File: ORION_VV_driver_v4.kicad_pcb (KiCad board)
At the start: 4 copper layers, 52.4 x 123.1 mm, 146 parts, among them J11 Conn_01x02, J12 Conn_01x05, J13 Conn_01x05, J15 Conn_01x02, J2 Conn_01x04, J3 Conn_01x04, J4 Conn_01x06, J5 Conn_01x07, J6 Conn_01x07, Q1 IRF8721PBF-1, Q10 IRF8721PBF-1, Q11 IRF8721PBF-1, Q12 IRF8721PBF-1, Q2 IRF8721PBF-1, Q3 IRF8721PBF-1, Q4 IRF8721PBF-1, Q5 IRF8721PBF-1, Q6 IRF8721PBF-1, Q7 IRF8721PBF-1, Q8 IRF8721PBF-1, Q9 IRF8721PBF-1, SW1 SW_Push, SW2 SW_Push, SW3 SW_Push, SW4 SW_Push, SW5 SW_Push, U1 BD9G101G, U2 L78L33_SOT89, U3 MAX3051, U5 INA199, U6 INA199, Y1 Resonator

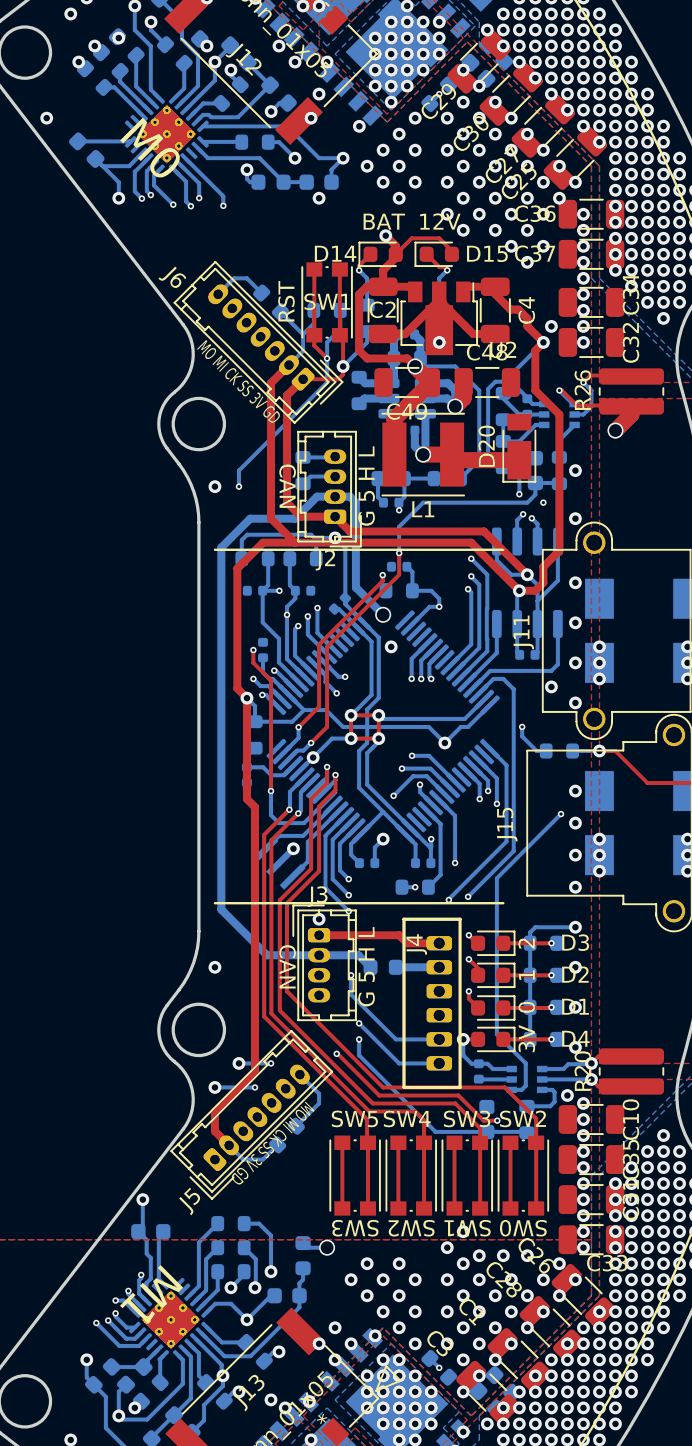
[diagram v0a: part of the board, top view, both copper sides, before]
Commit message: 配線とシルクの改善
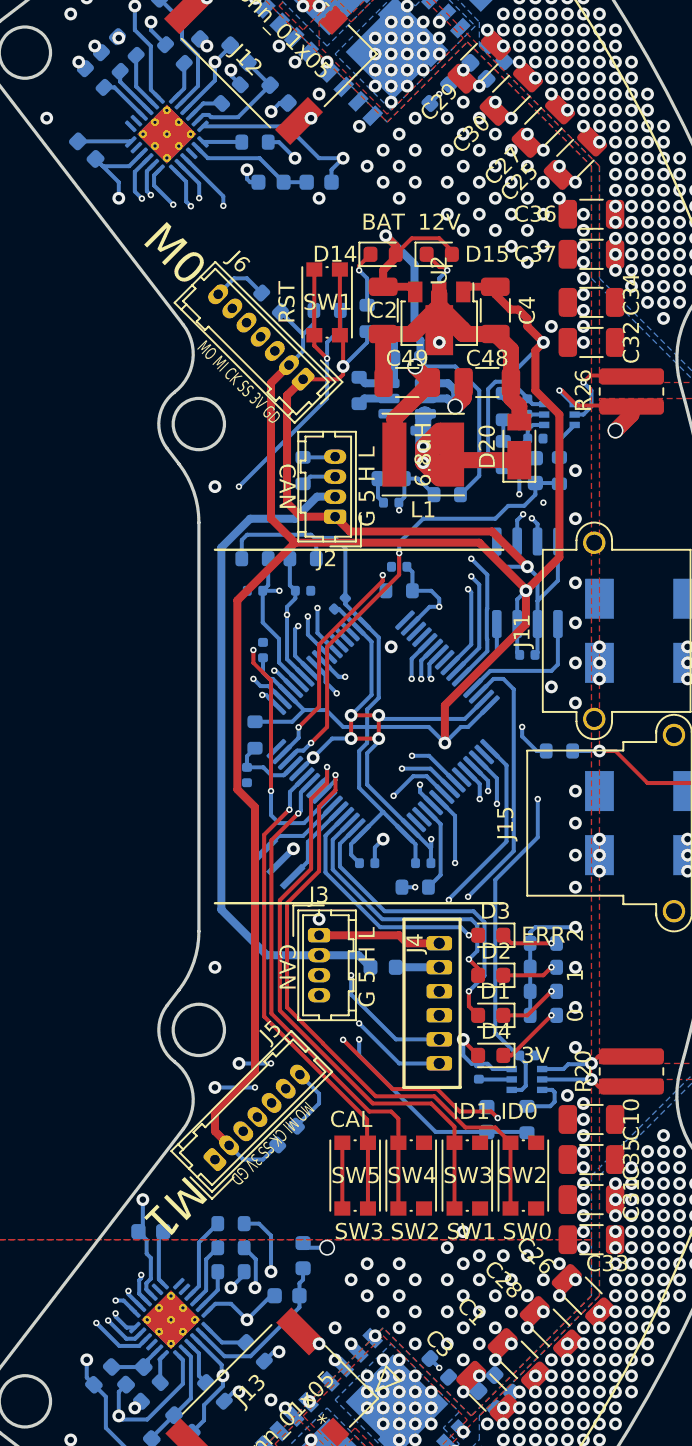
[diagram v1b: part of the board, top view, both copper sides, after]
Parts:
- added C53: 0.1u, Capacitor_SMD:C_0402_1005Metric, B.Cu at (121.0, 82.0)
- added C54: 0.1u, Capacitor_SMD:C_0402_1005Metric, B.Cu at (120.5, 120.5)
- moved R4 1.50 mm to (121.5, 118.0)
- moved D4 1.00 mm to (118.2, 120.5)
- moved R1 1.00 mm to (121.5, 116.5)
- moved R34 1.00 mm to (115.5, 85.5)
- moved D3 0.50 mm to (118.2, 113.0)
- moved R2 0.50 mm to (121.5, 115.0)
- moved D1 0.46 mm to (118.2, 118.0)
- turned SW2 to -90 degrees
- turned SW3 to -90 degrees
- turned SW4 to -90 degrees
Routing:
- net +5V: track 51.0 -> 41.8 mm, vias 1 -> 0
- net +3V3: track 206.0 -> 214.7 mm, vias 6 -> 4
- net GND: track 153.7 -> 159.4 mm
- net +BATT: track 48.4 -> 44.6 mm
- net Net-(C46-Pad1): track 10.5 -> 13.8 mm, vias 1 -> 2
- net /SW0: track 40.7 -> 38.9 mm
- net /SW2: track 33.2 -> 31.7 mm
- net /SW1: track 38.6 -> 37.0 mm
- net Net-(D4-Pad1): track 3.33 -> 4.36 mm
- net /LED_2: track 15.9 -> 15.1 mm, vias 2 -> 1
- net +9V: track 198.0 -> 197.2 mm
- net /TEMP_FET_1: track 67.1 -> 66.5 mm
- net Net-(D1-Pad1): track 3.34 -> 3.95 mm
- net /M0_CS: track 29.3 -> 28.7 mm
- net /LED_1: track 17.8 -> 17.4 mm, vias 2 -> 1
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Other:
- board text added: "6.8uH"
- board text added: "CAL"
- board text added: "ERR"
- board text added: "ID0"
- board text added: "ID1"

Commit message: 微調整
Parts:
- added J1: Conn_01x01, TestPoint:TestPoint_Pad_D1.0mm, F.Cu at (104.5, 69.5)
- added J10: Conn_01x01, TestPoint:TestPoint_Pad_D1.0mm, F.Cu at (103.0, 130.5)
- added J14: Conn_01x01, TestPoint:TestPoint_Pad_D1.0mm, F.Cu at (105.0, 130.5)
- added J7: Conn_01x01, TestPoint:TestPoint_Pad_D1.0mm, F.Cu at (102.5, 69.5)
- added J8: Conn_01x01, TestPoint:TestPoint_Pad_D1.0mm, F.Cu at (100.5, 69.5)
- added J9: Conn_01x01, TestPoint:TestPoint_Pad_D1.0mm, F.Cu at (101.0, 130.5)
- moved C14 2.06 mm to (118.5, 79.5)
- moved R9 2.06 mm to (118.5, 82.0)
- moved R8 1.12 mm to (118.5, 84.0), turned to 0 degrees
- moved C23 0.97 mm to (117.0, 124.5)
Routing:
- net /M1_WL: track 49.4 -> 60.2 mm
- net /M1_VL: track 51.0 -> 61.6 mm
- net /M1_UL: track 53.3 -> 63.2 mm
- net /M0_UL: track 43.6 -> 50.6 mm
- net /M0_VL: track 42.2 -> 48.9 mm
- net /M0_WL: track 41.7 -> 46.8 mm
- net GND: track 159.4 -> 160.6 mm
- net +9V: track 197.2 -> 196.4 mm
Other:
- board text added: "9V"
- board text added: "B"
- board text added: "G"
- board text added: "R"
- board text added: "UL VL WL"
- board text added: "W"
- board text removed: "12V"

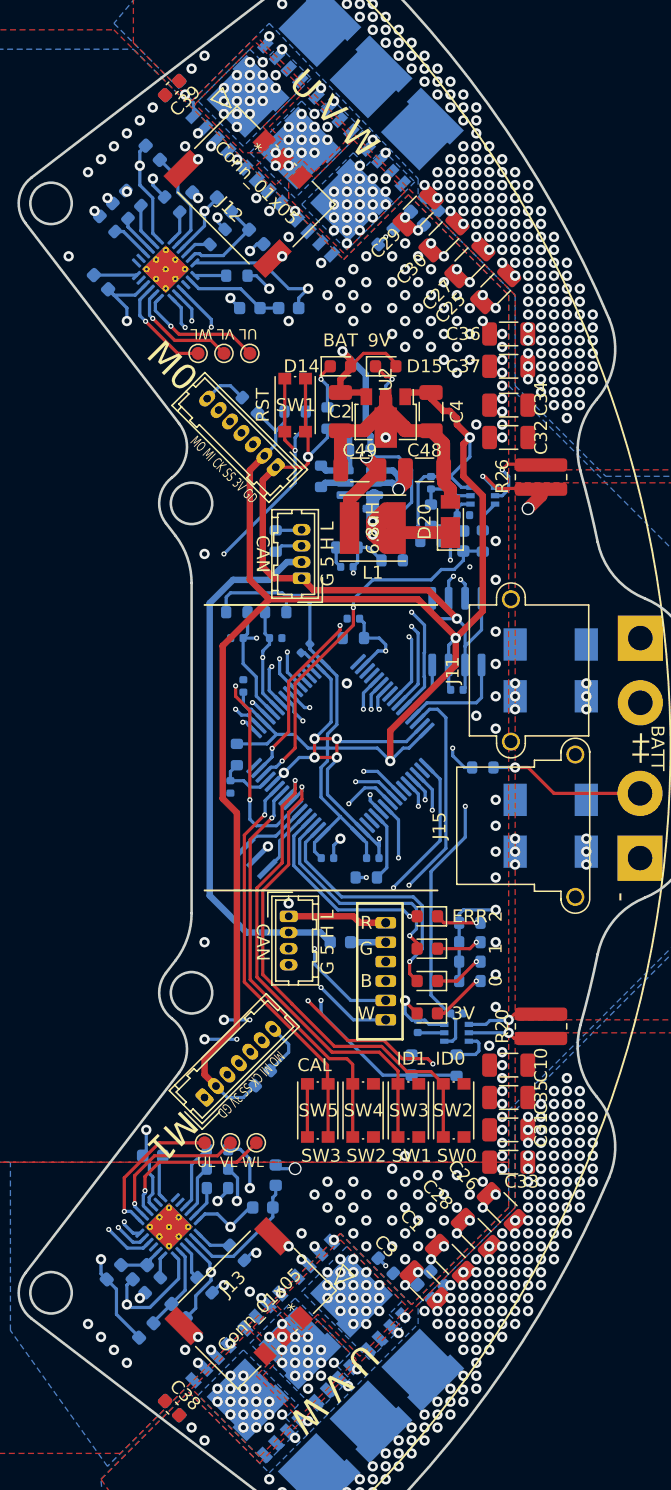
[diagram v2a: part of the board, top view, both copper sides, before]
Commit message: シルク追加
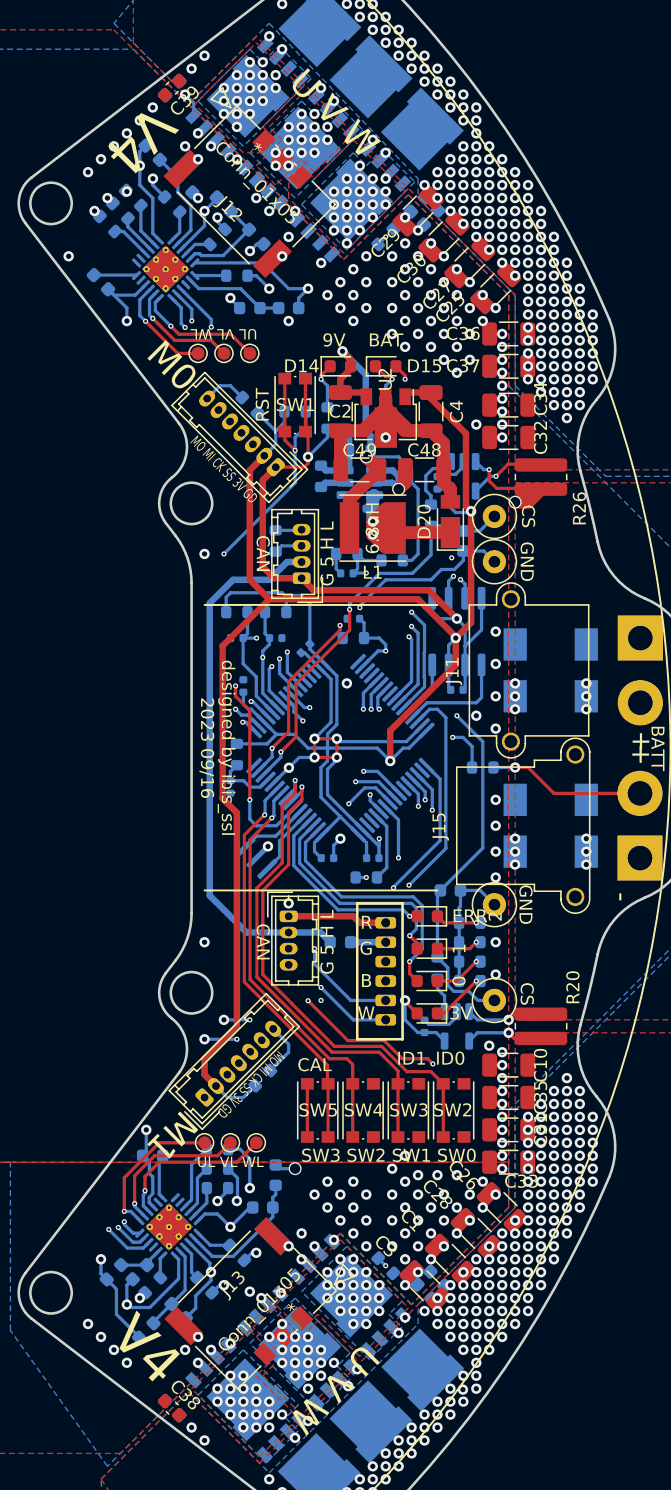
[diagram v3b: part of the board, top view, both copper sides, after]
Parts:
- removed C53, C54: 0.1u, Capacitor_SMD:C_0402_1005Metric
- removed R12, R13: 100, Resistor_SMD:R_0603_1608Metric
- added J16: Conn_01x01, TestPoint:TestPoint_Loop_D2.60mm_Drill0.9mm_Beaded, F.Cu at (123.4, 119.5)
- added J17: Conn_01x01, TestPoint:TestPoint_Loop_D2.60mm_Drill0.9mm_Beaded, F.Cu at (123.4, 85.6)
- added J18: Conn_01x01, TestPoint:TestPoint_Loop_D2.60mm_Drill0.9mm_Beaded, F.Cu at (123.4, 82.1)
- added J19: Conn_01x01, TestPoint:TestPoint_Loop_D2.60mm_Drill0.9mm_Beaded, F.Cu at (123.4, 112.1)
- C23, C24: value 1u -> 0.1u
- U5, U6: value INA199 -> ZXCT108x; footprint Package_TO_SOT_SMD:SOT-363_SC-70-6 -> Package_TO_SOT_SMD:SOT-23-5
- moved R8 33.0 mm to (119.0, 117.0), turned to -90 degrees
- moved C23 13.8 mm to (120.0, 111.0), turned to 0 degrees
- moved U6 2.12 mm to (121.0, 79.0), turned to -90 degrees
- moved C15 0.53 mm to (118.0, 121.5), turned to -90 degrees
- moved U5 0.50 mm to (120.5, 121.5), turned to -90 degrees
- moved C14 0.50 mm to (119.0, 79.5), turned to -90 degrees
- moved C50 0.50 mm to (112.0, 86.5)
- moved R35 0.50 mm to (112.0, 85.0)
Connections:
- C23 pad 1: GND -> /M1_CS
- C23 pad 2: /M1_CS -> GND
- C24 pad 1: GND -> /M0_CS
- C24 pad 2: /M0_CS -> GND
- D15 pad 2: +9V -> +BATT
- R8 pad 1: +3V3 -> /M1_CS
- R8 pad 2: /3V3_HARF_REF -> Net-(R8-Pad2)
- R9 pad 1: /3V3_HARF_REF -> /M0_CS
- R9 pad 2: GND -> Net-(R9-Pad2)
- U5 pad 1: /3V3_HARF_REF -> Net-(R8-Pad2)
- U5 pad 3: +3V3 -> +BATT
- U5 pad 4: +BATT -> /M1_CSL
- U5 pad 5: /M1_CSL -> +3V3
- U6 pad 1: /3V3_HARF_REF -> Net-(R9-Pad2)
- U6 pad 3: +3V3 -> +BATT
- U6 pad 4: +BATT -> /M0_CSL
- U6 pad 5: /M0_CSL -> +3V3
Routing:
- net /3V3_HARF_REF: track 49.5 -> 0.00 mm, vias 2 -> 0
- net GND: track 160.6 -> 175.3 mm, vias 174 -> 172
- net +BATT: track 44.6 -> 54.3 mm, vias 17 -> 18
- net +3V3: track 214.6 -> 205.4 mm
- net /M1_CS: track 44.9 -> 52.9 mm
- net Net-(R9-Pad2): track 0.00 -> 4.84 mm
- net +9V: track 196.4 -> 192.8 mm
- net Net-(R12-Pad2): track 3.28 -> 0.00 mm
- net /M0_CS: track 28.7 -> 31.6 mm
- net Net-(R8-Pad2): track 0.00 -> 2.77 mm
- net Net-(R13-Pad2): track 2.42 -> 0.00 mm
- net /GD_V_SENS: track 22.7 -> 23.4 mm
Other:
- board text added: "CS"
- board text added: "GND"
- board text added: "V4"
- board text added: "designed by ibis_ssl 2023 09/16"

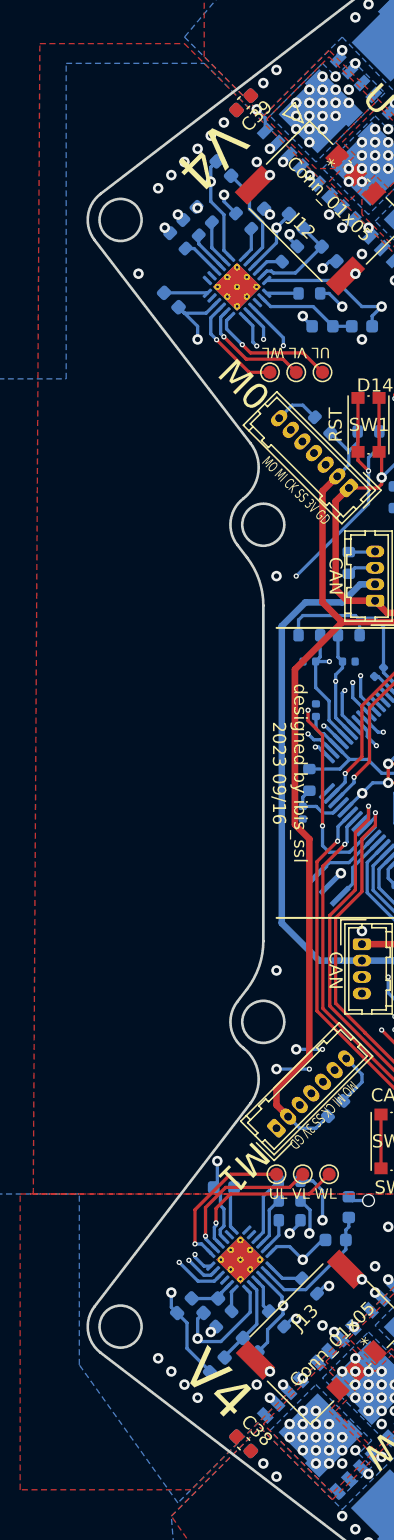
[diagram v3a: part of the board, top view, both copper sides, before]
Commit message: シルクをv4.1に修正
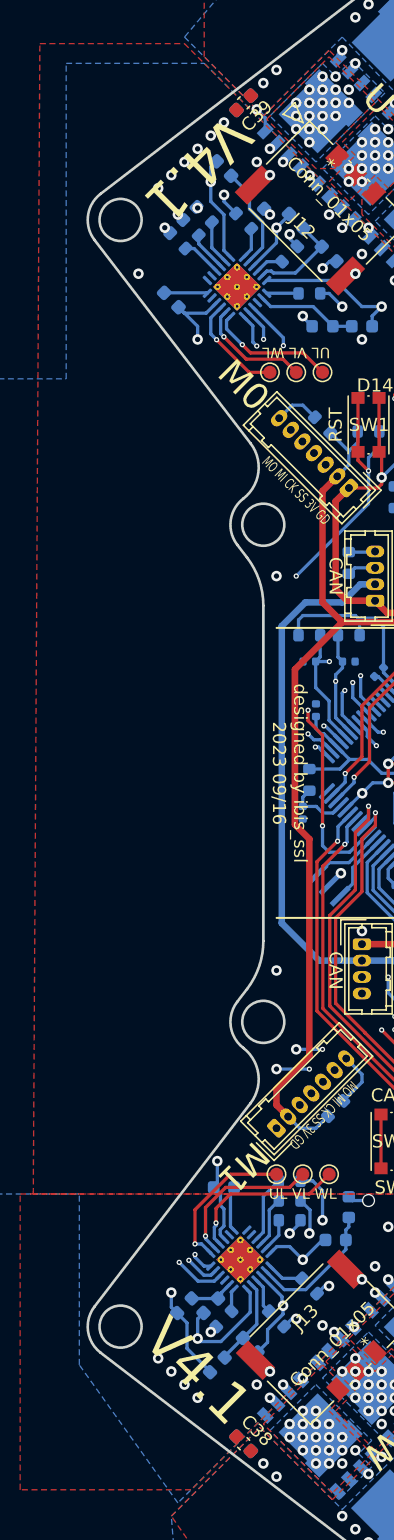
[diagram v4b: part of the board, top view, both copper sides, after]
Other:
- board text added: "V4.1"
- board text removed: "V4"
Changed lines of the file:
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@@
     (effects (font (size 1 1) (thickness 0.15)))
   )
-  (gr_text "V4" (at 96 53 225) (layer "F.SilkS")
+  (gr_text "V4.1" (at 95 54 225) (layer "F.SilkS")
     (effects (font (size 3 3) (thickness 0.5)))
   )
@@
     (effects (font (size 2 2) (thickness 0.3)))
   )
-  (gr_text "V4" (at 96.5 146.5 315) (layer "F.SilkS")
+  (gr_text "V4.1" (at 95 145.5 315) (layer "F.SilkS")
     (effects (font (size 3 3) (thickness 0.5)))
   )

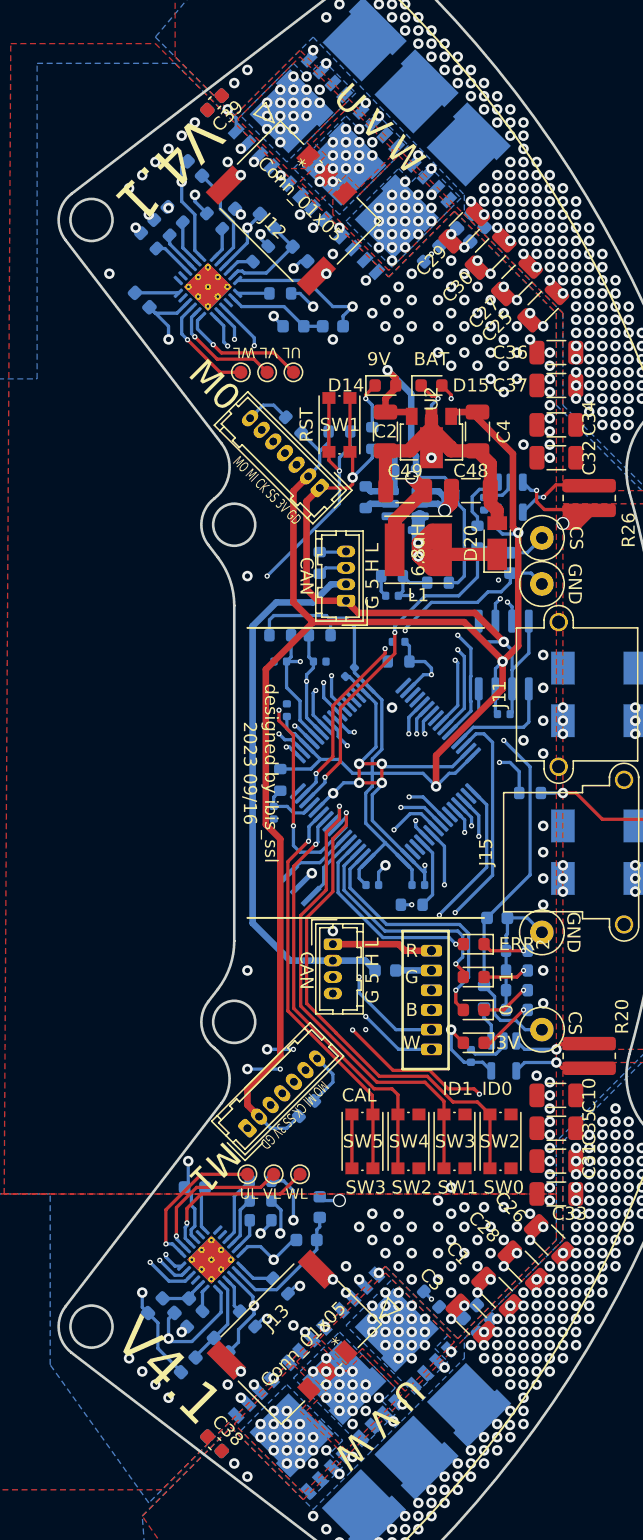
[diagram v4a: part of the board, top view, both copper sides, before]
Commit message: マイコン位置を変更&再配線中
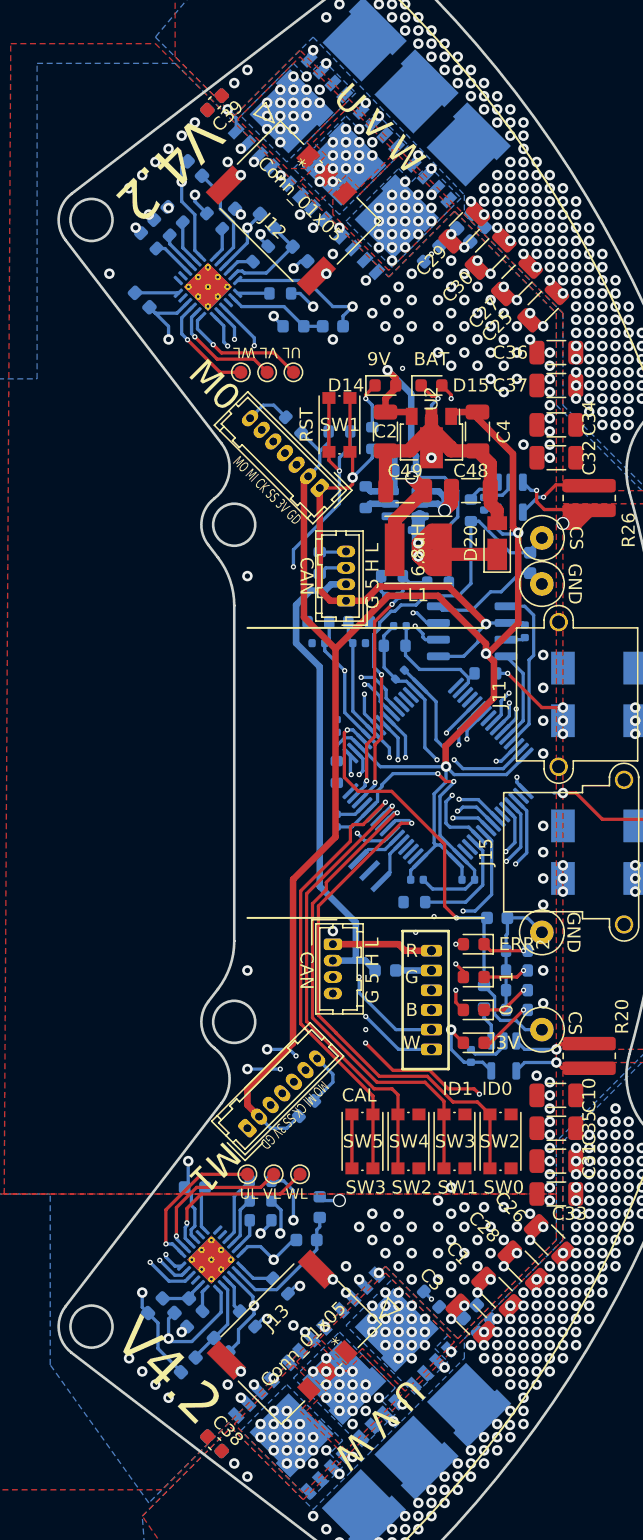
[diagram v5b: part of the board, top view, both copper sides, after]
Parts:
- moved R10 9.71 mm to (119.1, 92.4)
- moved C6 7.31 mm to (117.8, 108.1)
- moved C9 6.50 mm to (122.1, 89.2), turned to -90 degrees
- moved Y1 5.41 mm to (110.3, 107.4)
- moved C11 4.84 mm to (107.8, 103.6)
- moved FB1 4.34 mm to (107.8, 99.9)
- moved U4 4.00 mm to (115.5, 100.0)
- moved C8 3.98 mm to (107.8, 96.4)
- moved C5 3.81 mm to (112.6, 92.5)
- moved C52 3.31 mm to (109.5, 90.1)
- moved C51 3.22 mm to (106.4, 90.1)
- moved R37 3.16 mm to (109.5, 88.5)
- moved R36 3.07 mm to (106.4, 88.5)
- moved U3 3.00 mm to (118.1, 89.2), turned to 180 degrees
- moved R9 2.06 mm to (118.0, 80.0)
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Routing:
- net +3V3: track 205.4 -> 166.8 mm
- net /LED_0: track 19.7 -> 1.74 mm
- net /M1_CS: track 52.9 -> 35.2 mm
- net /LED_1: track 17.4 -> 1.24 mm
- net /LED_2: track 15.1 -> 0.57 mm
- net /CAN_H: track 57.6 -> 46.6 mm
- net /BATT_V_SENS: track 19.1 -> 9.55 mm, vias 2 -> 0
- net /TEMP_FET_0: track 58.5 -> 49.5 mm
- net /CAN_L: track 60.5 -> 51.7 mm
- net GND: track 175.3 -> 169.4 mm, vias 172 -> 164
- net +BATT: track 54.3 -> 59.4 mm, vias 18 -> 19
- net +5V: track 41.8 -> 36.9 mm
- net /NSS_ENC1: track 30.2 -> 34.6 mm
- net /CAN_TX: track 8.44 -> 12.7 mm
- net /TEMP_1: track 32.1 -> 36.3 mm
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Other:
- board text added: "V4.2"
- board text removed: "V4.1"
- board text removed: "designed by ibis_ssl 2023 09/16"
